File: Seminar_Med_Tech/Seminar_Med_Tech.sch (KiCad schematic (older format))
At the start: 86 parts

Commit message: merge
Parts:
- removed R2: NI, symbol R_Variable
- added J?: CONN_02X08, symbol CONN_02X08
- added RV1: POT, symbol POT
- gave numbers to parts that had none: 31
- renumbered C6 to C1, C19 to C11, C18 to C12, C8 to C14, C12 to C15, C15 to C16, C5 to C17, C20 to C19, C4 to C2, C3 to C21, C13 to C22, C76 to C23, C77 to C24, C1 to C25, C33 to C26, C10 to C27, C95 to C28, C9 to C29, C2 to C30, C22 to C31, C21 to C32, C11 to C33, C16 to C4, C14 to C5, C7 to C6, C17 to C7, JP1 to JP2, JP1 to JP3, JP17 to JP4, JP18 to JP6, JP19 to JP7, R59 to R1, R3 to R12, R8 to R13, R5 to R14, R1 to R15, R6 to R16, R4 to R17, R7 to R18, R58 to R2, R60 to R3, R61 to R4, R62 to R5, R63 to R6, R64 to R7, R65 to R8, R66 to R9, TP3 to TP2, TP1 to TP3, TP2 to TP4, TP11 to TP5, TP12 to TP6
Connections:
- net labels added: DRDY2
- net labels removed: ECG_V15N, ECV_V15P, ReservedDRDY
- wire segments 553 -> 634
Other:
- moved on the sheet: U10, U11, U12, U13, U15, U16, U17, U9, U?

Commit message: Update
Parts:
- JP1: renamed from JP3; value NI -> Jumper
- JP16: renamed from JP2; value JP16 -> Jumper
- U1: value JP26 -> JP22
- U10: value JP27 -> JP31
- U11: value JP28 -> JP32
- U12: value JP29 -> JP33
- U13: value JP30 -> JP34
- U15: value JP31 -> JP35
- U16: value JP32 -> JP36
- U17: value JP33 -> JP37
- U2: value JP27 -> JP23
- U3: value JP28 -> JP24
- U4: value JP29 -> JP25
- U5: value JP30 -> JP26
- U6: value JP31 -> JP27
- U7: value JP32 -> JP28
- U8: value JP33 -> JP29
- U9: value JP26 -> JP30
- renumbered JP4 to JP17, JP6 to JP18, JP7 to JP19, JP1 to JP4, U14 to U1
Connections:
- net /PWDN: no longer U?.9
- net AGND: now also JP5.2
- net GND: no longer JP5.2
- net SPI_IN: no longer U1.34 (DIN), U18.34 (DIN)
- net WCT: now reaches JP16.1, U1.1 (IN1), U2.1 (IN1), U3.1 (IN1), U4.1 (IN1), U5.1 (IN1), U8.1 (IN1)
- new net: U1.34 (DIN), U18.34 (DIN)
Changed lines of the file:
@@
 $EndDescr
 $Comp
-L Jumper JP2
+L Jumper JP16
 U 1 1 5921B571
 P 3450 1175
-F 0 "JP2" H 3450 1325 50  0000 C CNN
-F 1 "JP16" H 3450 1095 50  0000 C CNN
+F 0 "JP16" H 3450 1325 50  0000 C CNN
+F 1 "Jumper" H 3450 1095 50  0000 C CNN
 F 2 "" H 3450 1175 50  0001 C CNN
 F 3 "" H 3450 1175 50  0001 C CNN
@@
 P 3450 1475
 F 0 "U1" H 3625 1600 39  0000 C CNN
-F 1 "JP26" H 3250 1600 60  0000 C CNN
+F 1 "JP22" H 3250 1600 60  0000 C CNN
 F 2 "" H 3450 1475 60  0001 C CNN
 F 3 "" H 3450 1475 60  0001 C CNN
@@
 P 3450 1725
 F 0 "U2" H 3625 1850 60  0000 C CNN
-F 1 "JP27" H 3275 1850 60  0000 C CNN
+F 1 "JP23" H 3275 1850 60  0000 C CNN
 F 2 "" H 3450 1725 60  0001 C CNN
 F 3 "" H 3450 1725 60  0001 C CNN
@@
 P 3450 1975
 F 0 "U3" H 3625 2100 60  0000 C CNN
-F 1 "JP28" H 3275 2100 60  0000 C CNN
+F 1 "JP24" H 3275 2100 60  0000 C CNN
 F 2 "" H 3450 1975 60  0001 C CNN
 F 3 "" H 3450 1975 60  0001 C CNN
@@
 P 3450 2225
 F 0 "U4" H 3625 2350 60  0000 C CNN
-F 1 "JP29" H 3275 2350 60  0000 C CNN
+F 1 "JP25" H 3275 2350 60  0000 C CNN
 F 2 "" H 3450 2225 60  0001 C CNN
 F 3 "" H 3450 2225 60  0001 C CNN
@@
 P 3450 2500
 F 0 "U5" H 3625 2625 60  0000 C CNN
-F 1 "JP30" H 3275 2625 60  0000 C CNN
+F 1 "JP26" H 3275 2625 60  0000 C CNN
 F 2 "" H 3450 2500 60  0001 C CNN
 F 3 "" H 3450 2500 60  0001 C CNN
@@
 P 3450 2775
 F 0 "U6" H 3600 2900 60  0000 C CNN
-F 1 "JP31" H 3275 2900 60  0000 C CNN
+F 1 "JP27" H 3275 2900 60  0000 C CNN
 F 2 "" H 3450 2775 60  0001 C CNN
 F 3 "" H 3450 2775 60  0001 C CNN
@@
 P 3450 3050
 F 0 "U7" H 3625 3200 60  0000 C CNN
-F 1 "JP32" H 3275 3200 60  0000 C CNN
+F 1 "JP28" H 3275 3200 60  0000 C CNN
 F 2 "" H 3450 3050 60  0001 C CNN
 F 3 "" H 3450 3050 60  0001 C CNN
@@
 P 3450 3350
 F 0 "U8" H 3625 3500 60  0000 C CNN
-F 1 "JP33" H 3275 3500 60  0000 C CNN
+F 1 "JP29" H 3275 3500 60  0000 C CNN
 F 2 "" H 3450 3350 60  0001 C CNN
 F 3 "" H 3450 3350 60  0001 C CNN
@@
 AVSS
 $Comp
-L ADS1298 U14
+L ADS1298 U1
 U 1 1 5921E8FA
 P 5125 2425
-F 0 "U14" H 5575 1800 60  0000 C CNN
+F 0 "U1" H 5575 1800 60  0000 C CNN
 F 1 "ADS1298" H 5125 2525 60  0000 C CNN
 F 2 "" H 5075 2275 60  0001 C CNN
@@
 Text GLabel 9350 2800 2    39   Input ~ 0
 SPI_CS1
-Text GLabel 9800 2925 2    39   Input ~ 0
+Text GLabel 9825 2975 2    39   Input ~ 0
 SPI_IN
 Text GLabel 7200 2575 2    39   Input ~ 0
@@
 	0    1    1    0
 $EndComp
-$Comp
-L GND #PWR6
-U 1 1 592B55D3
-P 9125 6200
-F 0 "#PWR6" H 9125 5950 50  0001 C CNN
-F 1 "GND" H 9125 6050 50  0000 C CNN
-F 2 "" H 9125 6200 50  0001 C CNN
-F 3 "" H 9125 6200 50  0001 C CNN
-	1    9125 6200
-	0    -1   -1   0
-$EndComp
 Text Label 9025 4325 0    60   ~ 0
 DVDD
@@
 $EndComp
 $Comp
-L Jumper JP1
+L Jumper JP4
 U 1 1 592BD318
 P 2625 5350
-F 0 "JP1" H 2625 5500 50  0000 C CNN
+F 0 "JP4" H 2625 5500 50  0000 C CNN
 F 1 "Jumper" H 2625 5270 50  0000 C CNN
 F 2 "" H 2625 5350 50  0001 C CNN
@@
 PACEOUT12
 Text GLabel 10600 4950 2    60   Input ~ 0
-/PWDN
-Text GLabel 10600 5075 2    60   Input ~ 0
 /PWDN
 Text GLabel 10100 4575 0    60   Input ~ 0
@@
 $EndComp
 $Comp
-L Jumper_NC_Dual JP4
+L Jumper_NC_Dual JP17
 U 1 1 59389AEC
 P 6825 850
-F 0 "JP4" H 6875 750 50  0000 L CNN
+F 0 "JP17" H 6875 750 50  0000 L CNN
 F 1 "NI" H 6825 950 50  0000 C BNN
 F 2 "" H 6825 850 50  0001 C CNN
@@
 U 1 1 5938E491
 P 4725 1425
-F 0 "R12" V 4800 1575 50  0000 C CNN
+F 0 "R12" V 4600 1425 50  0000 C CNN
 F 1 "0" V 4725 1425 50  0000 C CNN
 F 2 "" V 4655 1425 50  0001 C CNN
@@
 $EndComp
 $Comp
-L Jumper_NC_Small JP3
+L Jumper_NC_Small JP1
 U 1 1 59391637
 P 4875 1425
-F 0 "JP3" H 4875 1375 50  0000 C CNN
-F 1 "NI" H 5000 1375 50  0000 C CNN
+F 0 "JP1" H 4750 1375 50  0000 C CNN
+F 1 "Jumper" H 5000 1375 50  0000 C CNN
 F 2 "" H 4875 1425 50  0001 C CNN
 F 3 "" H 4875 1425 50  0001 C CNN
@@
 AVSS
 $Comp
-L Jumper_NC_Dual JP6
+L Jumper_NC_Dual JP18
 U 1 1 593C6B14
 P 9500 2300
-F 0 "JP6" H 9550 2200 50  0000 L CNN
+F 0 "JP18" H 9550 2200 50  0000 L CNN
 F 1 "NI" H 9500 2400 50  0000 C BNN
 F 2 "" H 9500 2300 50  0001 C CNN
@@
 $EndComp
 $Comp
-L Jumper_NC_Dual JP7
+L Jumper_NC_Dual JP19
 U 1 1 593CE6F6
 P 11075 1825
-F 0 "JP7" H 11125 1725 50  0000 L CNN
+F 0 "JP19" H 11125 1725 50  0000 L CNN
 F 1 "NI" H 11075 1925 50  0000 C BNN
 F 2 "" H 11075 1825 50  0001 C CNN
@@
 P 5025 4550
 F 0 "U9" H 5200 4675 39  0000 C CNN
-F 1 "JP26" H 4825 4675 60  0000 C CNN
+F 1 "JP30" H 4825 4675 60  0000 C CNN
 F 2 "" H 5025 4550 60  0001 C CNN
 F 3 "" H 5025 4550 60  0001 C CNN
@@
 P 5025 4800
 F 0 "U10" H 5200 4925 60  0000 C CNN
-F 1 "JP27" H 4850 4925 60  0000 C CNN
+F 1 "JP31" H 4850 4925 60  0000 C CNN
 F 2 "" H 5025 4800 60  0001 C CNN
 F 3 "" H 5025 4800 60  0001 C CNN
@@
 P 5025 5050
 F 0 "U11" H 5200 5175 60  0000 C CNN
-F 1 "JP28" H 4850 5175 60  0000 C CNN
+F 1 "JP32" H 4850 5175 60  0000 C CNN
 F 2 "" H 5025 5050 60  0001 C CNN
 F 3 "" H 5025 5050 60  0001 C CNN
@@
 P 5025 5300
 F 0 "U12" H 5200 5425 60  0000 C CNN
-F 1 "JP29" H 4850 5425 60  0000 C CNN
+F 1 "JP33" H 4850 5425 60  0000 C CNN
 F 2 "" H 5025 5300 60  0001 C CNN
 F 3 "" H 5025 5300 60  0001 C CNN
@@
 P 5025 5575
 F 0 "U13" H 5200 5700 60  0000 C CNN
-F 1 "JP30" H 4850 5700 60  0000 C CNN
+F 1 "JP34" H 4850 5700 60  0000 C CNN
 F 2 "" H 5025 5575 60  0001 C CNN
 F 3 "" H 5025 5575 60  0001 C CNN
@@
 P 5025 5850
 F 0 "U15" H 5175 5975 60  0000 C CNN
-F 1 "JP31" H 4850 5975 60  0000 C CNN
+F 1 "JP35" H 4850 5975 60  0000 C CNN
 F 2 "" H 5025 5850 60  0001 C CNN
 F 3 "" H 5025 5850 60  0001 C CNN
@@
 P 5025 6125
 F 0 "U16" H 5200 6275 60  0000 C CNN
-F 1 "JP32" H 4850 6275 60  0000 C CNN
+F 1 "JP36" H 4850 6275 60  0000 C CNN
 F 2 "" H 5025 6125 60  0001 C CNN
 F 3 "" H 5025 6125 60  0001 C CNN
@@
 P 5025 6425
 F 0 "U17" H 5200 6575 60  0000 C CNN
-F 1 "JP33" H 4850 6575 60  0000 C CNN
+F 1 "JP37" H 4850 6575 60  0000 C CNN
 F 2 "" H 5025 6425 60  0001 C CNN
 F 3 "" H 5025 6425 60  0001 C CNN
@@
 	6950 2925 8950 2925
 Wire Wire Line
-	8950 2925 9800 2925
+	8975 2975 9825 2975
 Connection ~ 8950 2925
 Wire Wire Line
@@
 Wire Wire Line
 	5100 7600 5500 7600
+Text Label 9125 6200 0    60   ~ 0
+AGND
+Text Label 3050 1175 0    60   ~ 0
+WCT
 $EndSCHEMATC

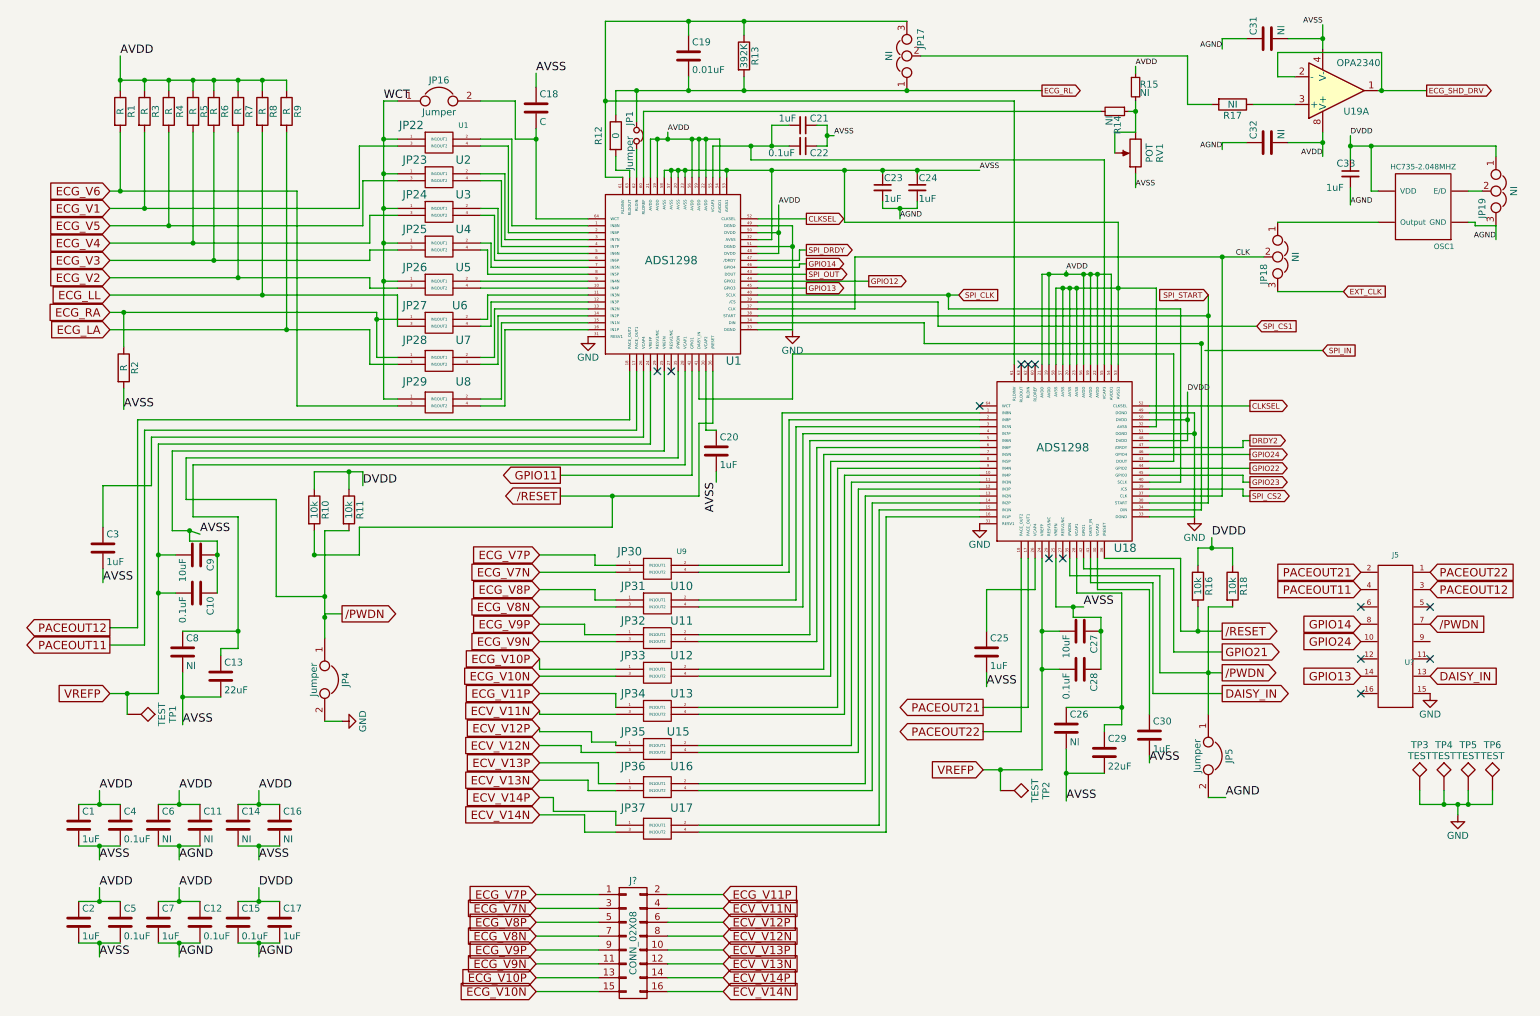
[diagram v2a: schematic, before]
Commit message: Changed components list
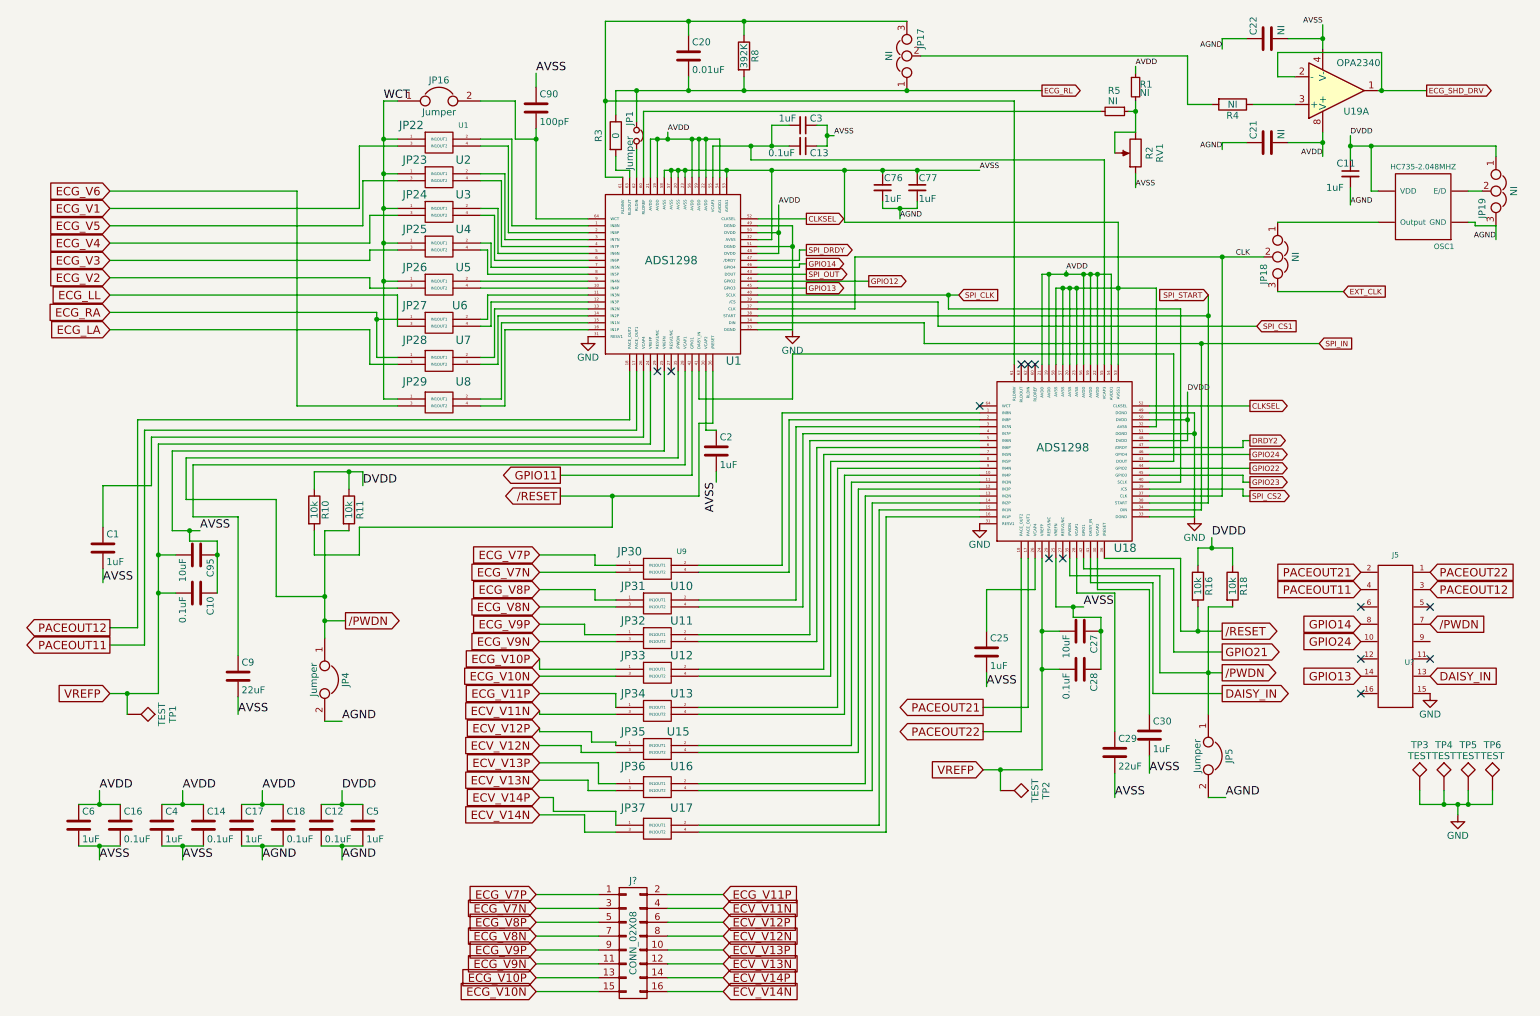
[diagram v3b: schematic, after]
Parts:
- removed C11, C14, C16, C6: NI, symbol C
- removed C26, C8: Nl, symbol C
- removed R1, R2, R3, R4, R5, R6, R7, R8, R9: R, symbol R
- C90: renamed from C18; value C -> 100pF
- RV1: value POT -> R2
- renumbered C3 to C1, C33 to C11, C15 to C12, C22 to C13, C5 to C14, C4 to C16, C7 to C17, C12 to C18, C20 to C2, C19 to C20, C32 to C21, C31 to C22, C21 to C3, C2 to C4, C17 to C5, C1 to C6, C23 to C76, C24 to C77, C13 to C9, C9 to C95, R15 to R1, R12 to R3, R17 to R4, R14 to R5, R13 to R8
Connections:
- net AGND: now also JP4.2
- net GND: no longer JP4.2
- net SPI_IN: now also U1.34 (DIN), U18.34 (DIN)
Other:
- moved on the sheet: C12, C14, C17, C18, C29, C4, C5, C9

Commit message: Update
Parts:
- gave numbers to parts that had none: 2
- renumbered U1 to U20
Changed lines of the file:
@@
 AVSS
 $Comp
-L ADS1298 U1
+L ADS1298 U20
 U 1 1 5921E8FA
 P 5125 2425
-F 0 "U1" H 5575 1800 60  0000 C CNN
+F 0 "U20" H 5575 1800 60  0000 C CNN
 F 1 "ADS1298" H 5125 2525 60  0000 C CNN
 F 2 "" H 5075 2275 60  0001 C CNN
@@
 $EndComp
 $Comp
-L GND #PWR4
+L GND #PWR01
 U 1 1 5922AF93
 P 7350 4225
-F 0 "#PWR4" H 7350 3975 50  0001 C CNN
+F 0 "#PWR01" H 7350 3975 50  0001 C CNN
 F 1 "GND" H 7350 4075 50  0000 C CNN
 F 2 "" H 7350 4225 50  0001 C CNN
@@
 CLK
 $Comp
-L GND #PWR2
+L GND #PWR02
 U 1 1 592AF0AE
 P 4525 2875
-F 0 "#PWR2" H 4525 2625 50  0001 C CNN
+F 0 "#PWR02" H 4525 2625 50  0001 C CNN
 F 1 "GND" H 4525 2725 50  0000 C CNN
 F 2 "" H 4525 2875 50  0001 C CNN
@@
 NoConn ~ 7350 3375
 $Comp
-L GND #PWR3
+L GND #PWR03
 U 1 1 592C9248
 P 6000 2825
-F 0 "#PWR3" H 6000 2575 50  0001 C CNN
+F 0 "#PWR03" H 6000 2575 50  0001 C CNN
 F 1 "GND" H 6000 2675 50  0000 C CNN
 F 2 "" H 6000 2825 50  0001 C CNN
@@
 $EndComp
 $Comp
-L GND #PWR5
+L GND #PWR04
 U 1 1 592C92E3
 P 8900 4175
-F 0 "#PWR5" H 8900 3925 50  0001 C CNN
+F 0 "#PWR04" H 8900 3925 50  0001 C CNN
 F 1 "GND" H 8900 4025 50  0000 C CNN
 F 2 "" H 8900 4175 50  0001 C CNN
@@
 $EndComp
 $Comp
-L Header12 U?
+L Header12 U14
 U 1 1 592B1741
 P 10350 4900
-F 0 "U?" H 10450 4575 39  0000 C CNN
+F 0 "U14" H 10450 4575 39  0000 C CNN
 F 1 "J5" H 10350 5350 39  0000 C CNN
 F 2 "" H 10350 4925 60  0001 C CNN
@@
 NoConn ~ 10100 4825
 $Comp
-L GND #PWR?
+L GND #PWR05
 U 1 1 592B1F34
 P 10600 5450
-F 0 "#PWR?" H 10600 5200 50  0001 C CNN
+F 0 "#PWR05" H 10600 5200 50  0001 C CNN
 F 1 "GND" H 10600 5300 50  0000 C CNN
 F 2 "" H 10600 5450 50  0001 C CNN
@@
 $EndComp
 $Comp
-L GND #PWR8
+L GND #PWR06
 U 1 1 592B54F4
 P 10800 6325
-F 0 "#PWR8" H 10800 6075 50  0001 C CNN
+F 0 "#PWR06" H 10800 6075 50  0001 C CNN
 F 1 "GND" H 10800 6175 50  0000 C CNN
 F 2 "" H 10800 6325 50  0001 C CNN
@@
 $EndComp
 $Comp
-L CONN_02X08 J?
+L CONN_02X08 J1
 U 1 1 594C2861
 P 4850 7250
-F 0 "J?" H 4850 7700 50  0000 C CNN
+F 0 "J1" H 4850 7700 50  0000 C CNN
 F 1 "CONN_02X08" V 4850 7250 50  0000 C CNN
 F 2 "" H 4850 6050 50  0001 C CNN
